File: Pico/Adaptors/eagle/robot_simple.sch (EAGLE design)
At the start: 30 parts, among them J1 JST-2P-SMD-PW-3410050P1, SW1 3010010P1,MS-22D18,JS202011CQN, U3 MAX1555

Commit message: rotate ultrasonic, add fast charge
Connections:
- net 5V: now also U3.DC
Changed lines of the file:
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@@
 <grid distance="0.1" unitdist="inch" unit="inch" style="lines" multiple="1" display="no" altdistance="0.01" altunitdist="inch" altunit="inch"/>
 <layers>
-<layer number="1" name="Top" color="4" fill="1" visible="yes" active="no"/>
-<layer number="16" name="Bottom" color="1" fill="1" visible="yes" active="no"/>
-<layer number="17" name="Pads" color="2" fill="1" visible="yes" active="no"/>
-<layer number="18" name="Vias" color="2" fill="1" visible="yes" active="no"/>
-<layer number="19" name="Unrouted" color="6" fill="1" visible="yes" active="no"/>
-<layer number="20" name="Dimension" color="15" fill="1" visible="yes" active="no"/>
-<layer number="21" name="tPlace" color="7" fill="1" visible="yes" active="no"/>
-<layer number="22" name="bPlace" color="7" fill="1" visible="yes" active="no"/>
-<layer number="23" name="tOrigins" color="15" fill="1" visible="yes" active="no"/>
-<layer number="24" name="bOrigins" color="15" fill="1" visible="yes" active="no"/>
-<layer number="25" name="tNames" color="7" fill="1" visible="yes" active="no"/>
-<layer number="26" name="bNames" color="7" fill="1" visible="yes" active="no"/>
-<layer number="27" name="tValues" color="7" fill="1" visible="yes" active="no"/>
-<layer number="28" name="bValues" color="7" fill="1" visible="yes" active="no"/>
+<layer number="1" name="Top" color="4" fill="1" visible="no" active="no"/>
+<layer number="16" name="Bottom" color="1" fill="1" visible="no" active="no"/>
+<layer number="17" name="Pads" color="2" fill="1" visible="no" active="no"/>
+<layer number="18" name="Vias" color="2" fill="1" visible="no" active="no"/>
+<layer number="19" name="Unrouted" color="6" fill="1" visible="no" active="no"/>
+<layer number="20" name="Dimension" color="15" fill="1" visible="no" active="no"/>
+<layer number="21" name="tPlace" color="7" fill="1" visible="no" active="no"/>
+<layer number="22" name="bPlace" color="7" fill="1" visible="no" active="no"/>
+<layer number="23" name="tOrigins" color="15" fill="1" visible="no" active="no"/>
+<layer number="24" name="bOrigins" color="15" fill="1" visible="no" active="no"/>
+<layer number="25" name="tNames" color="7" fill="1" visible="no" active="no"/>
+<layer number="26" name="bNames" color="7" fill="1" visible="no" active="no"/>
+<layer number="27" name="tValues" color="7" fill="1" visible="no" active="no"/>
+<layer number="28" name="bValues" color="7" fill="1" visible="no" active="no"/>
 <layer number="29" name="tStop" color="7" fill="3" visible="no" active="no"/>
 <layer number="30" name="bStop" color="7" fill="6" visible="no" active="no"/>
@@
 <layer number="35" name="tGlue" color="7" fill="4" visible="no" active="no"/>
 <layer number="36" name="bGlue" color="7" fill="5" visible="no" active="no"/>
-<layer number="37" name="tTest" color="7" fill="1" visible="yes" active="no"/>
-<layer number="38" name="bTest" color="7" fill="1" visible="yes" active="no"/>
+<layer number="37" name="tTest" color="7" fill="1" visible="no" active="no"/>
+<layer number="38" name="bTest" color="7" fill="1" visible="no" active="no"/>
 <layer number="39" name="tKeepout" color="4" fill="11" visible="no" active="no"/>
 <layer number="40" name="bKeepout" color="1" fill="11" visible="no" active="no"/>
@@
 <layer number="44" name="Drills" color="7" fill="1" visible="no" active="no"/>
 <layer number="45" name="Holes" color="7" fill="1" visible="no" active="no"/>
-<layer number="46" name="Milling" color="3" fill="1" visible="yes" active="no"/>
-<layer number="47" name="Measures" color="7" fill="1" visible="yes" active="no"/>
-<layer number="48" name="Document" color="7" fill="1" visible="yes" active="no"/>
-<layer number="49" name="Reference" color="7" fill="1" visible="yes" active="no"/>
-<layer number="50" name="dxf" color="7" fill="1" visible="yes" active="no"/>
-<layer number="51" name="tDocu" color="7" fill="1" visible="yes" active="no"/>
-<layer number="52" name="bDocu" color="7" fill="1" visible="yes" active="no"/>
-<layer number="53" name="tGND_GNDA" color="7" fill="9" visible="yes" active="no"/>
-<layer number="54" name="bGND_GNDA" color="1" fill="9" visible="yes" active="no"/>
-<layer number="56" name="wert" color="7" fill="1" visible="yes" active="no"/>
+<layer number="46" name="Milling" color="3" fill="1" visible="no" active="no"/>
+<layer number="47" name="Measures" color="7" fill="1" visible="no" active="no"/>
+<layer number="48" name="Document" color="7" fill="1" visible="no" active="no"/>
+<layer number="49" name="Reference" color="7" fill="1" visible="no" active="no"/>
+<layer number="50" name="dxf" color="7" fill="1" visible="no" active="no"/>
+<layer number="51" name="tDocu" color="7" fill="1" visible="no" active="no"/>
+<layer number="52" name="bDocu" color="7" fill="1" visible="no" active="no"/>
+<layer number="53" name="tGND_GNDA" color="7" fill="9" visible="no" active="no"/>
+<layer number="54" name="bGND_GNDA" color="1" fill="9" visible="no" active="no"/>
+<layer number="56" name="wert" color="7" fill="1" visible="no" active="no"/>
 <layer number="91" name="Nets" color="2" fill="1" visible="yes" active="yes"/>
 <layer number="92" name="Busses" color="1" fill="1" visible="yes" active="yes"/>
@@
 <wire x1="172.72" y1="116.84" x2="180.34" y2="116.84" width="0.1524" layer="91"/>
 <junction x="172.72" y="116.84"/>
-</segment>
-<segment>
+<pinref part="U3" gate="G$1" pin="DC"/>
+<wire x1="149.86" y1="124.46" x2="154.94" y2="124.46" width="0.1524" layer="91"/>
+<wire x1="154.94" y1="124.46" x2="154.94" y2="116.84" width="0.1524" layer="91"/>
+</segment>
+<segment>

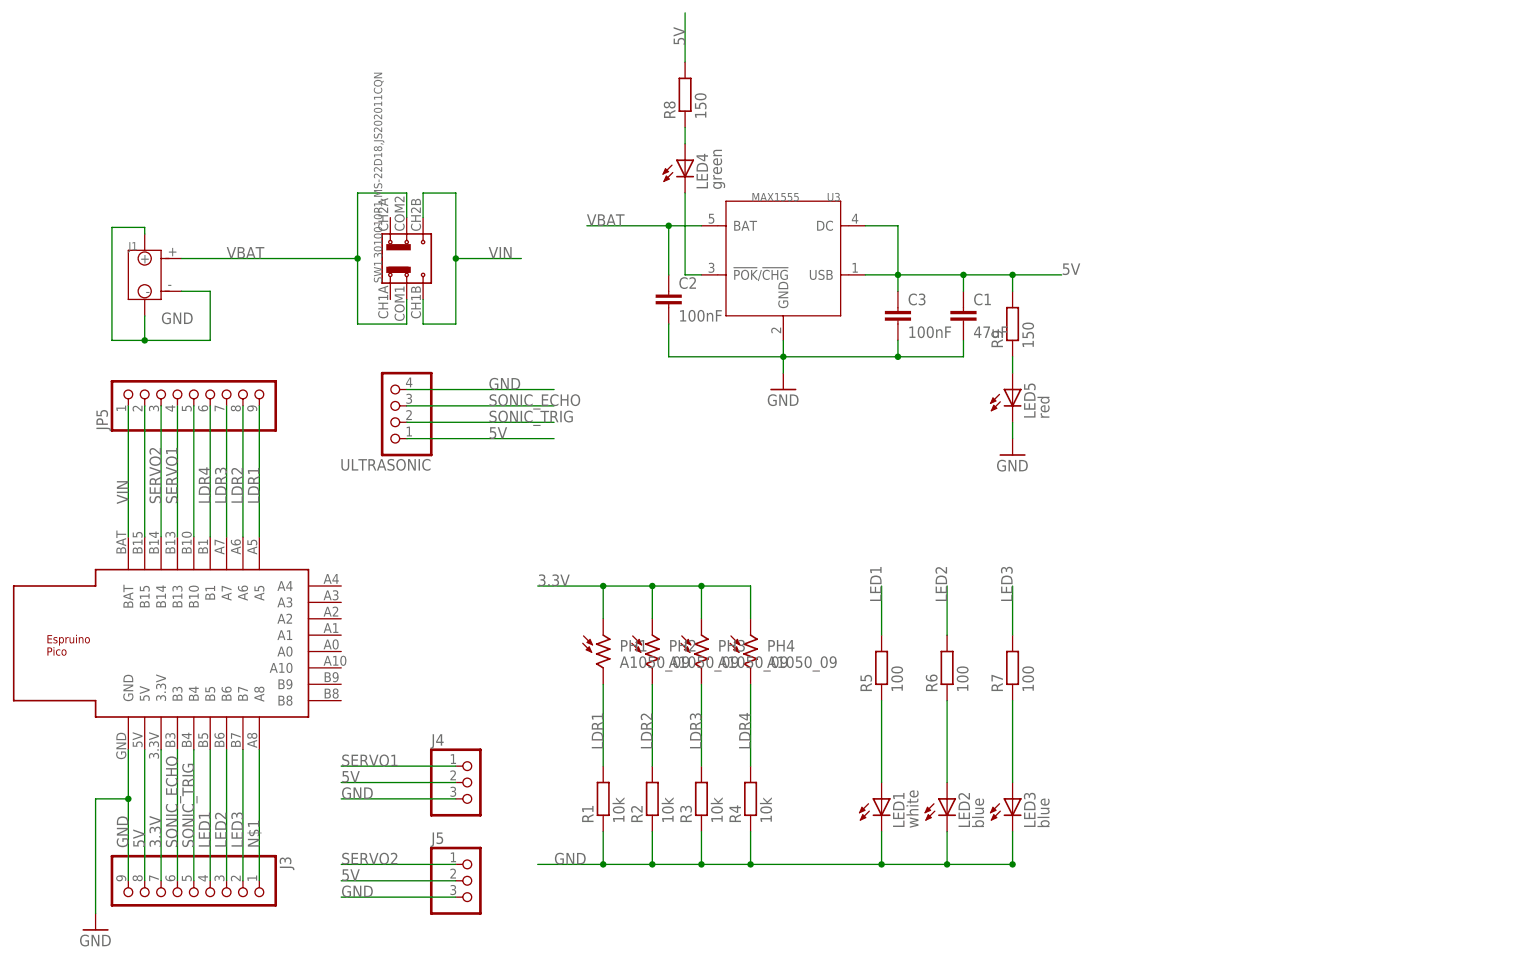
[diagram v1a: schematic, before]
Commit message: tweaked robot design - swap LEDs, add optional bluetooth
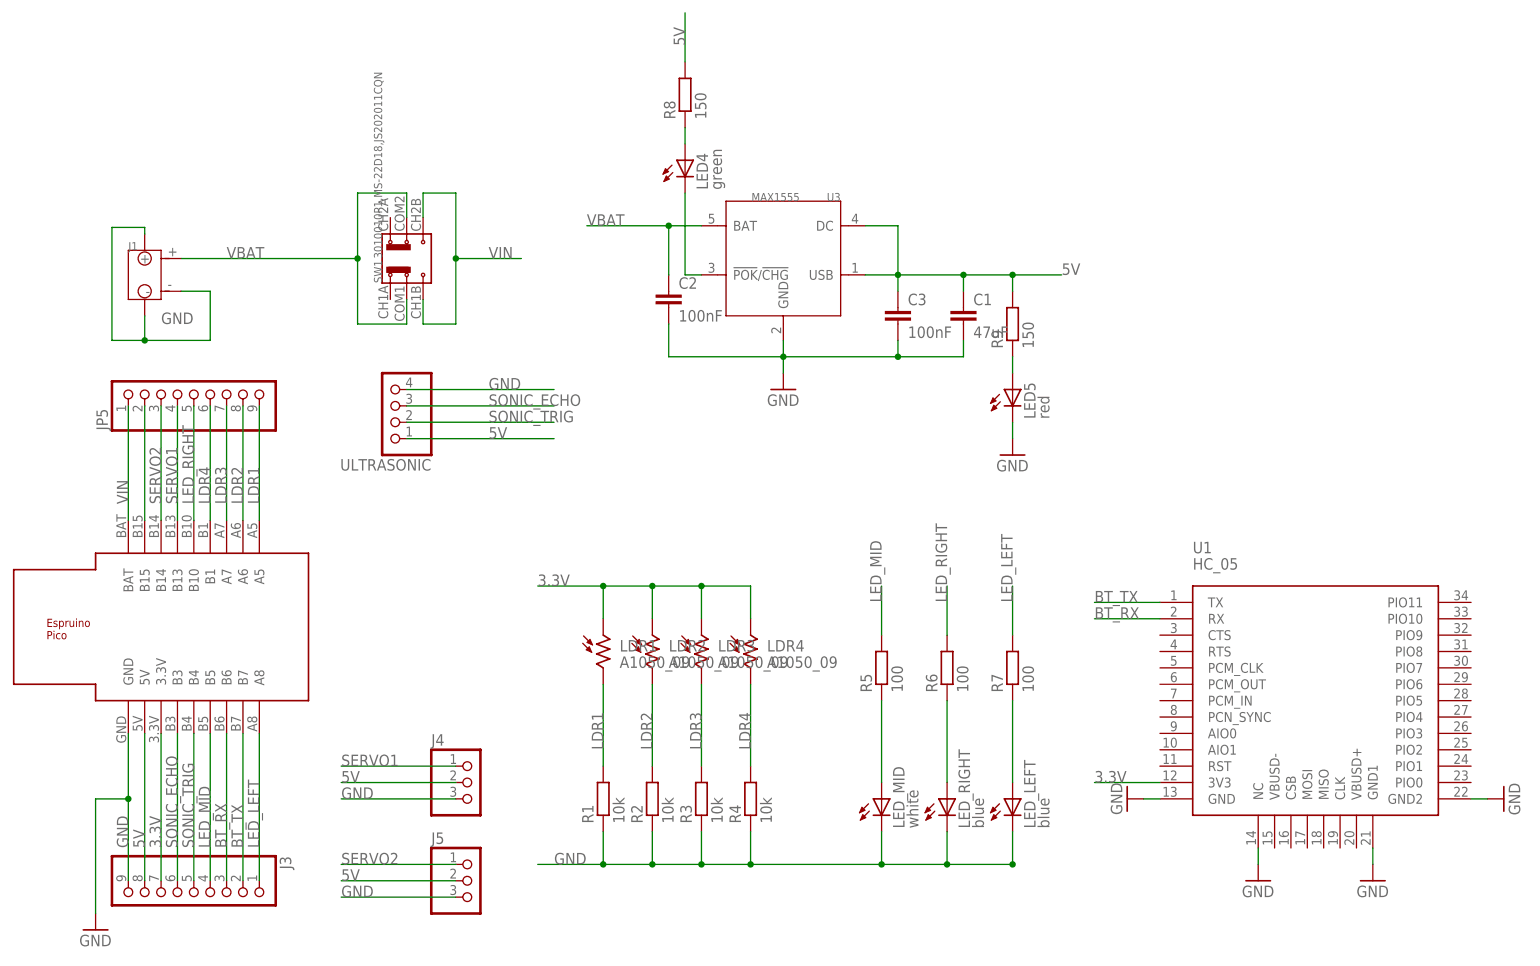
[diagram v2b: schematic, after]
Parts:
- added U1: HC_05, bluetooth:HC_05
- U$1: value ESPRUINO_PICO_HALFSMD -> ESPRUINO_PICO_0.1; device espruino_pico:ESPRUINO_PICO_HALFSMD -> espruino_pico:ESPRUINO_PICO_0.1
- renumbered LED1 to LED_MID, LED2 to LED_RIGHT, LED3 to LED_LEFT, PH1 to LDR1, PH2 to LDR2, PH3 to LDR3, PH4 to LDR4
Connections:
- net LED1 renamed LED_MID
- removed net $N52: JP5.5, U$1.B10
- removed net LED2: J3.3, R6.2, U$1.B6
- removed net LED3: J3.2, R7.2, U$1.B7
- removed net N$1: J3.1, U$1.A8
- new net BT_RX: J3.3, U$1.B6, U1.RX
- new net BT_TX: J3.2, U$1.B7, U1.TX
- new net LED_LEFT: J3.1, R7.2, U$1.A8
- new net LED_RIGHT: JP5.5, R6.2, U$1.B10
- net 3.3V: now also U1.3V3
- net GND: now also U1.GND, U1.GND1, U1.GND2, U1.NC
